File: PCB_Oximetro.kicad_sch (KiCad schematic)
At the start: 22 parts, among them J2 Conn_01x08, J3 USB_B_Micro, SW1 SW_Push, U1 LM1117MP-1.8, U2 MAX30102, U3 LM1117MP-3.3, U5 ESP32-DEVKIT-V1

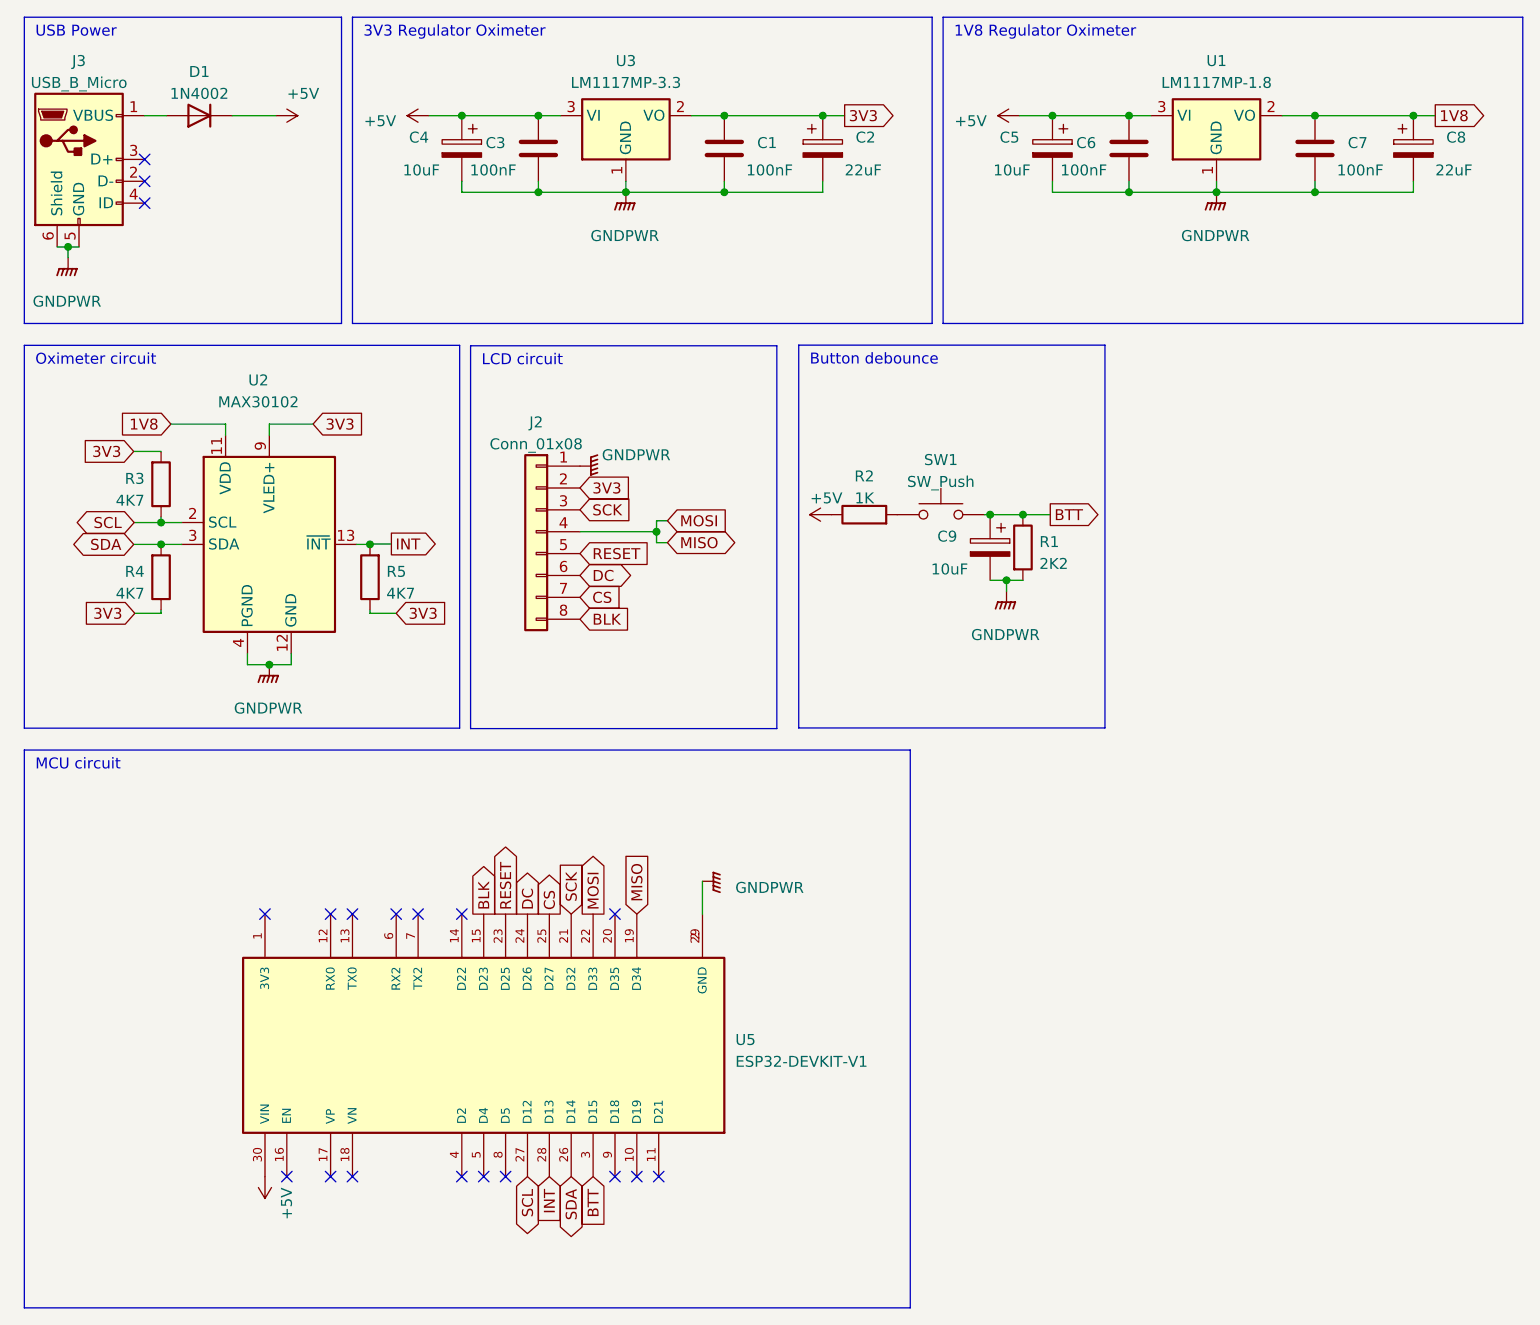
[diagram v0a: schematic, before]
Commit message: Oximeter change
Removed MAX30102 sensor and added MAX30102 shield
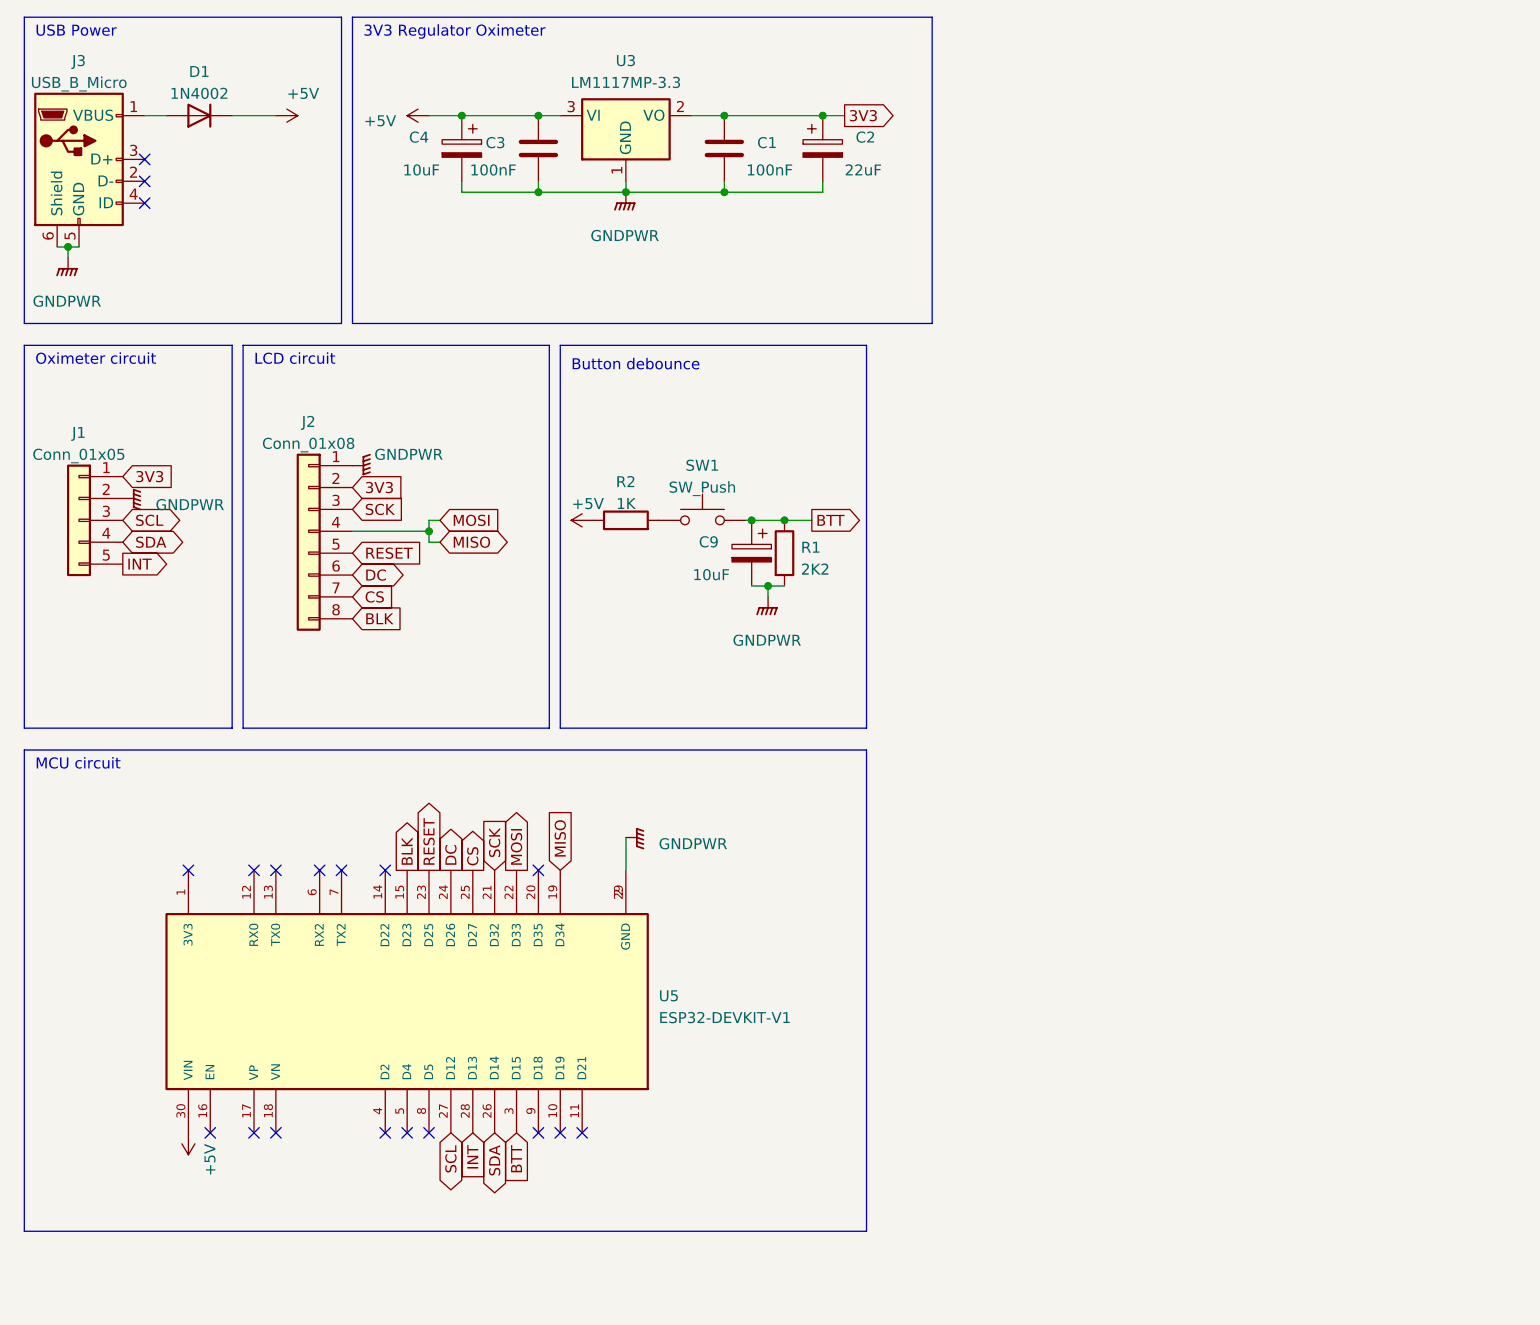
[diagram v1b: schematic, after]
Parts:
- removed C5: 10uF, Capacitor_THT:CP_Radial_D5.0mm_P2.50mm, symbol Device:C_Polarized
- removed C6, C7: 100nF, Capacitor_SMD:C_1206_3216Metric, symbol Device:C
- removed C8: 22uF, Capacitor_THT:CP_Radial_Tantal_D5.0mm_P2.50mm, symbol Device:C_Polarized
- removed R3, R4, R5: 4K7, Resistor_SMD:R_1206_3216Metric, symbol Device:R
- removed U1: LM1117MP-1.8, Package_TO_SOT_SMD:SOT-223-3_TabPin2, symbol Regulator_Linear:LM1117MP-1.8
- removed U2: MAX30102, OptoDevice:Maxim_OLGA-14_3.3x5.6mm_P0.8mm, symbol Sensor:MAX30102
- added J1: Conn_01x05, Connector_PinSocket_2.54mm:PinSocket_1x06_P2.54mm_Vertical, symbol Connector_Generic:Conn_01x05
- J3: footprint (none) -> Connector_USB:USB_Micro-B_Amphenol_10104110_Horizontal
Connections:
- net 3V3: now also J1.1 (Pin_1)
- net GNDPWR: now also J1.2 (Pin_2)
- net INT: now also J1.5 (Pin_5)
- net SCL: now also J1.3 (Pin_3)
- net SDA: now also J1.4 (Pin_4)
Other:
- note removed: "1V8 Regulator Oximeter"
- moved on the sheet: C9, J2, R1, R2, SW1, U5

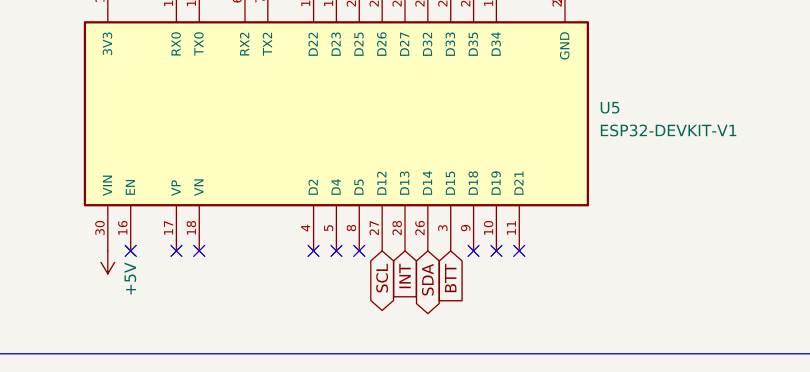
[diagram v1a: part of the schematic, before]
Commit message: PCB Layout
Changed pcb layout for MAX30102 module
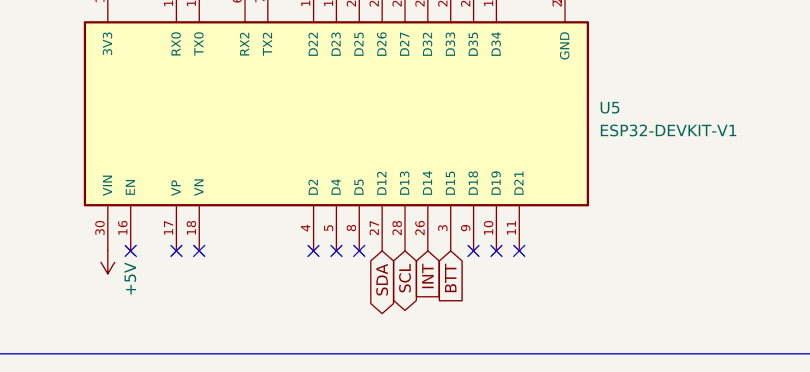
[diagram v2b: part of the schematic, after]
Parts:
- J1: footprint Connector_PinSocket_2.54mm:PinSocket_1x06_P2.54mm_Vertical -> Connector_PinSocket_2.54mm:PinSocket_1x05_P2.54mm_Vertical
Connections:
- net INT: now also U5.26 (D14); no longer U5.28 (D13)
- net SCL: now also U5.28 (D13); no longer U5.27 (D12)
- net SDA: now also U5.27 (D12); no longer U5.26 (D14)
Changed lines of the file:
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@@
     )
   )
-  (global_label "SCL" (shape bidirectional) (at 66.04 147.32 270) (fields_autoplaced)
+  (global_label "SCL" (shape bidirectional) (at 68.58 147.32 270) (fields_autoplaced)
     (effects (font (size 1.27 1.27)) (justify right))
-    (property "Intersheetrefs" "${INTERSHEET_REFS}" (at 66.04 154.8447 90)
+    (property "Intersheetrefs" "${INTERSHEET_REFS}" (at 68.58 154.8447 90)
       (effects (font (size 1.27 1.27)) (justify right) hide)
     )
@@
     )
   )
-  (global_label "INT" (shape input) (at 68.58 147.32 270) (fields_autoplaced)
+  (global_label "INT" (shape input) (at 71.12 147.32 270) (fields_autoplaced)
     (effects (font (size 1.27 1.27)) (justify right))
-    (property "Intersheetrefs" "${INTERSHEET_REFS}" (at 68.58 153.1287 90)
+    (property "Intersheetrefs" "${INTERSHEET_REFS}" (at 71.12 153.1287 90)
       (effects (font (size 1.27 1.27)) (justify right) hide)
     )
   )
-  (global_label "SDA" (shape bidirectional) (at 71.12 147.32 270) (fields_autoplaced)
+  (global_label "SDA" (shape bidirectional) (at 66.04 147.32 270) (fields_autoplaced)
     (effects (font (size 1.27 1.27)) (justify right))
-    (property "Intersheetrefs" "${INTERSHEET_REFS}" (at 71.12 154.9052 90)
+    (property "Intersheetrefs" "${INTERSHEET_REFS}" (at 66.04 154.9052 90)
       (effects (font (size 1.27 1.27)) (justify right) hide)
     )
@@
       (effects (font (size 1.27 1.27)))
     )
-    (property "Footprint" "Connector_PinSocket_2.54mm:PinSocket_1x06_P2.54mm_Vertical" (at 22.86 76.2 0)
-      (effects (font (size 1.27 1.27)) hide)
-    )
+    (property "Footprint" "Connector_PinSocket_2.54mm:PinSocket_1x05_P2.54mm_Vertical" (at 22.86 76.2 0)
+      (effects (font (size 1.27 1.27)) hide)
+    )

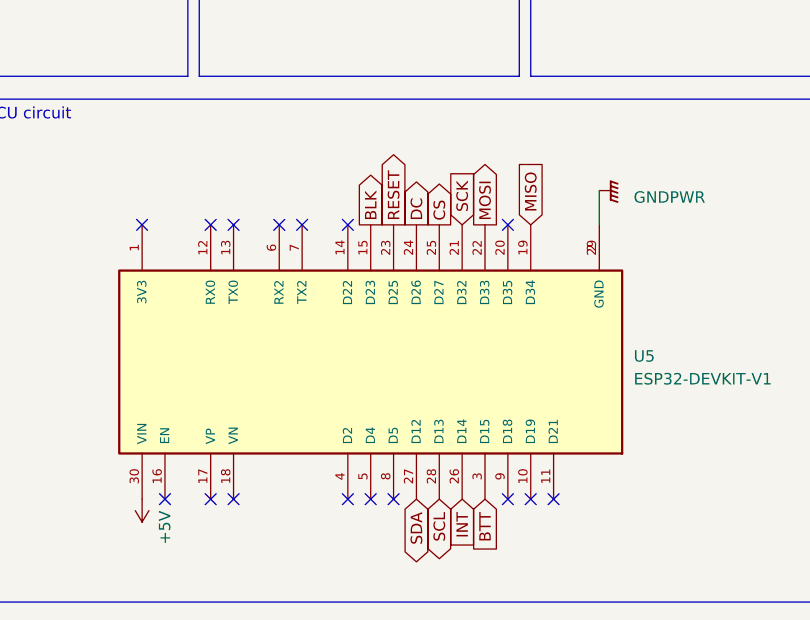
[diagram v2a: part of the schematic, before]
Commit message: GPIO12 change
GPIO12 change because of ESP32 boot
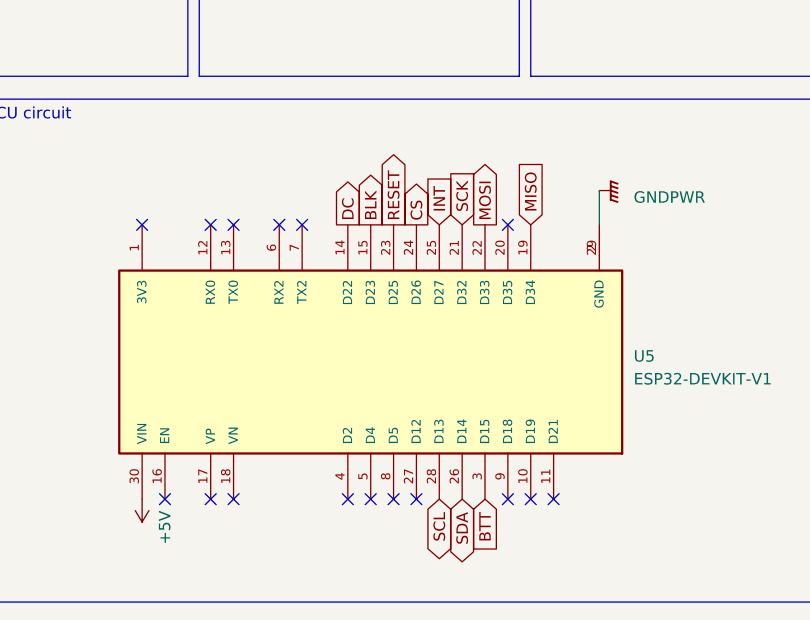
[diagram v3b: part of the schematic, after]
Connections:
- net CS: now also U5.24 (D26); no longer U5.25 (D27)
- net DC: now also U5.14 (D22); no longer U5.24 (D26)
- net INT: now also U5.25 (D27); no longer U5.26 (D14)
- net SDA: now also U5.26 (D14); no longer U5.27 (D12)
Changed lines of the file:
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@@
   (no_connect (at 53.34 116.84))
   (no_connect (at 43.18 116.84))
-  (no_connect (at 58.42 116.84))
+  (no_connect (at 63.5 147.32))
   (no_connect (at 43.18 147.32))
   (no_connect (at 30.48 39.37))
@@
   (no_connect (at 60.96 147.32))
   (no_connect (at 30.48 36.83))
-  (no_connect (at 63.5 147.32))
+  (no_connect (at 66.04 147.32))
   (no_connect (at 35.56 116.84))
   (wire (pts (xy 64.77 76.2) (xy 63.5 76.2))
@@
     )
   )
-  (global_label "CS" (shape output) (at 68.58 116.84 90) (fields_autoplaced)
-    (effects (font (size 1.27 1.27)) (justify left))
-    (property "Intersheetrefs" "${INTERSHEET_REFS}" (at 68.58 111.4547 90)
+  (global_label "CS" (shape output) (at 66.04 116.84 90) (fields_autoplaced)
+    (effects (font (size 1.27 1.27)) (justify left))
+    (property "Intersheetrefs" "${INTERSHEET_REFS}" (at 66.04 111.4547 90)
       (effects (font (size 1.27 1.27)) (justify left) hide)
     )
@@
     )
   )
-  (global_label "DC" (shape output) (at 66.04 116.84 90) (fields_autoplaced)
-    (effects (font (size 1.27 1.27)) (justify left))
-    (property "Intersheetrefs" "${INTERSHEET_REFS}" (at 66.04 111.3942 90)
+  (global_label "DC" (shape output) (at 58.42 116.84 90) (fields_autoplaced)
+    (effects (font (size 1.27 1.27)) (justify left))
+    (property "Intersheetrefs" "${INTERSHEET_REFS}" (at 58.42 111.3942 90)
       (effects (font (size 1.27 1.27)) (justify left) hide)
     )
@@
     )
   )
-  (global_label "INT" (shape input) (at 71.12 147.32 270) (fields_autoplaced)
+  (global_label "INT" (shape input) (at 68.58 116.84 90) (fields_autoplaced)
+    (effects (font (size 1.27 1.27)) (justify left))
+    (property "Intersheetrefs" "${INTERSHEET_REFS}" (at 68.58 111.0313 90)
+      (effects (font (size 1.27 1.27)) (justify left) hide)
+    )
+  )
+  (global_label "SDA" (shape bidirectional) (at 71.12 147.32 270) (fields_autoplaced)
     (effects (font (size 1.27 1.27)) (justify right))
-    (property "Intersheetrefs" "${INTERSHEET_REFS}" (at 71.12 153.1287 90)
+    (property "Intersheetrefs" "${INTERSHEET_REFS}" (at 71.12 154.9052 90)
       (effects (font (size 1.27 1.27)) (justify right) hide)
     )
-  )
-  (global_label "SDA" (shape bidirectional) (at 66.04 147.32 270) (fields_autoplaced)
-    (effects (font (size 1.27 1.27)) (justify right))
-    (property "Intersheetrefs" "${INTERSHEET_REFS}" (at 66.04 154.9052 90)
-      (effects (font (size 1.27 1.27)) (justify right) hide)
-    )

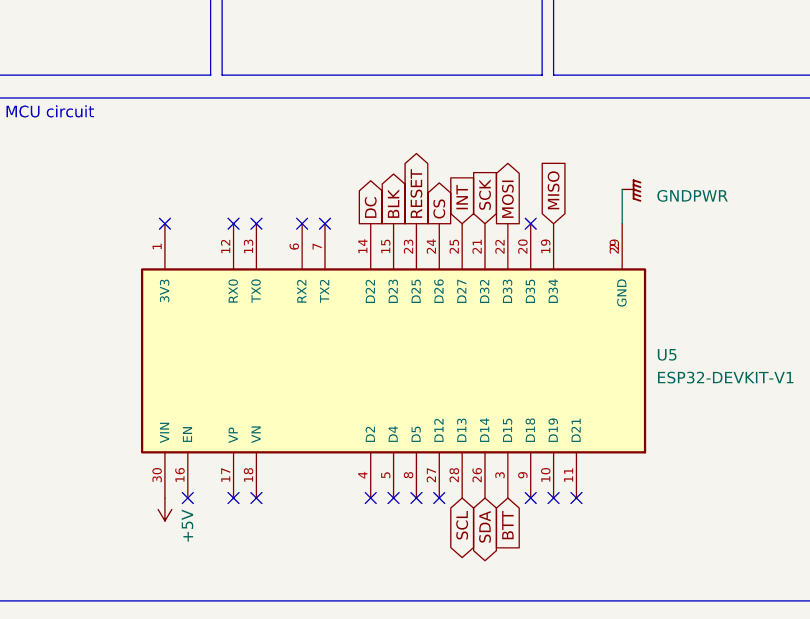
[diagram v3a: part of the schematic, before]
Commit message: BTT pin
Changed BTT pin because of boot
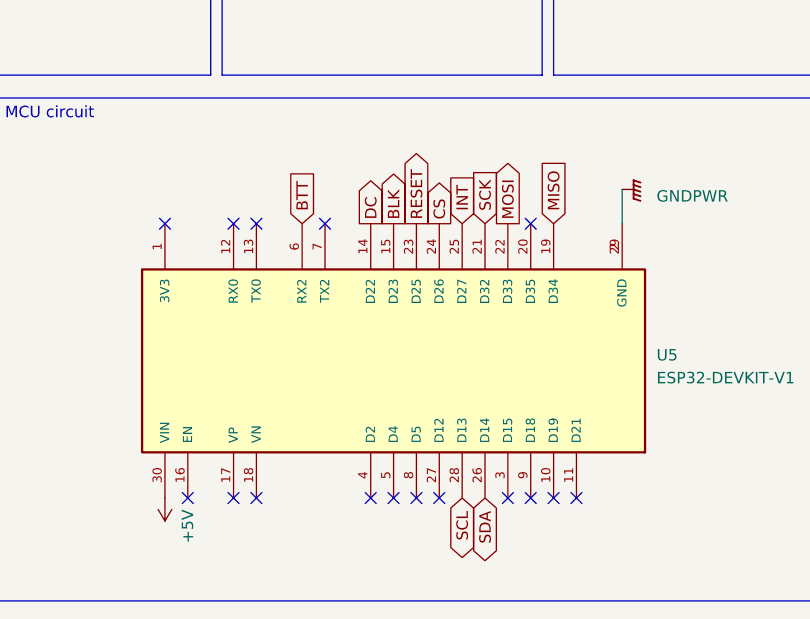
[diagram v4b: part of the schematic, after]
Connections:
- net BTT: now also U5.6 (RX2); no longer U5.3 (D15)
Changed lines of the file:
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@@
   (no_connect (at 53.34 116.84))
   (no_connect (at 43.18 116.84))
-  (no_connect (at 63.5 147.32))
+  (no_connect (at 73.66 147.32))
   (no_connect (at 43.18 147.32))
   (no_connect (at 30.48 39.37))
   (no_connect (at 30.48 34.29))
   (no_connect (at 78.74 147.32))
-  (no_connect (at 50.8 116.84))
+  (no_connect (at 60.96 147.32))
   (no_connect (at 76.2 116.84))
   (no_connect (at 38.1 147.32))
   (no_connect (at 81.28 147.32))
   (no_connect (at 58.42 147.32))
-  (no_connect (at 60.96 147.32))
+  (no_connect (at 63.5 147.32))
   (no_connect (at 30.48 36.83))
   (no_connect (at 66.04 147.32))
@@
     )
   )
-  (global_label "BTT" (shape input) (at 73.66 147.32 270) (fields_autoplaced)
-    (effects (font (size 1.27 1.27)) (justify right))
-    (property "Intersheetrefs" "${INTERSHEET_REFS}" (at 73.66 153.431 90)
-      (effects (font (size 1.27 1.27)) (justify right) hide)
-    )
-  )
+  (global_label "BTT" (shape input) (at 50.8 116.84 90) (fields_autoplaced)
+    (effects (font (size 1.27 1.27)) (justify left))
+    (property "Intersheetrefs" "${INTERSHEET_REFS}" (at 50.8 110.729 90)
+      (effects (font (size 1.27 1.27)) (justify left) hide)
+    )
+  )
